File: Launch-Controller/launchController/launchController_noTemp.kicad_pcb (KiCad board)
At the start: 4 copper layers, 226 x 138.5 mm, 103 parts, among them J1 Conn_01x05_Pin, J10 Conn_01x05_Pin, J11 Raspberry_Pi_5, J13 26 pin Dsub, J14 DB25_Plug, J16 DB25_Plug, J17 DB25_Plug, J2 Conn_01x05_Pin, J3 Conn_01x05_Pin, J4 Conn_01x05_Pin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

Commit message: dimensions
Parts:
- C10, C11, C12, C13, C14, C2, C3, C4, C5, C6, C7, C8, C9: footprint Capacitor_THT:C_Disc_D5.1mm_W3.2mm_P5.00mm -> Capacitor_SMD:C_0402_1005Metric_Pad0.74x0.62mm_HandSolder
- D1, D13, D14, D15, D16, D17, D18, D19, D20, D21, D22: footprint LED_THT:LED_D4.0mm -> LED_SMD:LED_1206_3216Metric_Pad1.42x1.75mm_HandSolder
- D10, D11, D12, D2, D3, D4, D5, D6, D7, D8, D9: footprint LED_THT:LED_D3.0mm -> LED_SMD:LED_0603_1608Metric_Pad1.05x0.95mm_HandSolder
- Q1, Q10, Q2, Q3, Q4, Q5, Q6, Q7, Q8, Q9: footprint Package_TO_SOT_THT:TO-220-3_Horizontal_TabDown -> Package_TO_SOT_SMD:SOT-23-3
- R1, R10, R11, R12, R3, R4, R5, R6, R7, R8, R9: footprint Resistor_THT:R_Axial_DIN0411_L9.9mm_D3.6mm_P12.70mm_Horizontal -> Resistor_SMD:R_0805_2012Metric_Pad1.20x1.40mm_HandSolder
- R13, R14, R15, R16, R17, R18, R19, R2, R20, R21, R22, R23, R24, R25, R26, R27, R28, R29, R30, R31, R32: footprint Resistor_THT:R_Axial_DIN0207_L6.3mm_D2.5mm_P7.62mm_Horizontal -> Resistor_SMD:R_1210_3225Metric_Pad1.30x2.65mm_HandSolder
- U1, U2: footprint SARP:ADS1015 -> launch_controller:ADS1115
- moved C13 161.3 mm to (381.7, 309.0), turned to 0 degrees
- moved C12 132.2 mm to (381.7, 307.1), turned to 0 degrees
- moved C14 106.8 mm to (381.7, 311.0), turned to 0 degrees
- moved H4 28.7 mm to (196.9, 371.5)
- moved H2 28.3 mm to (403.4, 371.5)
- moved R23 26.3 mm to (371.2, 308.2), turned to 0 degrees
- moved D13 26.1 mm to (211.3, 364.0), turned to -90 degrees
- moved D3 25.7 mm to (218.7, 365.7)
- moved D14 25.3 mm to (230.6, 364.0), turned to -90 degrees
- moved D4 24.7 mm to (238.0, 365.7)
- moved D15 24.7 mm to (250.0, 364.0), turned to -90 degrees
- moved R24 24.3 mm to (371.2, 312.4), turned to 0 degrees
- moved D16 24.1 mm to (269.4, 364.0), turned to -90 degrees
- moved D5 23.8 mm to (257.4, 365.7)
- moved D17 23.6 mm to (288.8, 364.0), turned to -90 degrees
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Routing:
- net /+5V: track 765.3 -> 213.6 mm
- net /RelayOut1: track 245.0 -> 7.23 mm, vias 2 -> 0
- net /RelayOut2: track 222.9 -> 7.23 mm, vias 2 -> 0
- net /RelayOut3: track 203.8 -> 7.23 mm, vias 2 -> 0
- net /RelayOut4: track 189.7 -> 7.23 mm, vias 2 -> 0
- net /RelayOut5: track 158.4 -> 7.23 mm
- net /RelayOut6: track 136.9 -> 7.23 mm
- net /GPIO 4: track 117.8 -> 0.00 mm
- net /RelayOut7: track 112.1 -> 7.23 mm
- net /GPIO 17: track 101.9 -> 0.00 mm
- net /GPIO 13: track 95.1 -> 0.00 mm
- net /GPIO 27: track 83.5 -> 0.00 mm
- net /RelayOut8: track 90.0 -> 7.23 mm
- net /GPIO 6: track 76.1 -> 0.00 mm
- net /PressureSwitch_in3: track 71.9 -> 0.00 mm
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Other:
- board size 226 x 138.5 mm -> 228.5 x 138.5 mm
- board text added: "IN"
- board text added: "OUT"

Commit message: fixed edge cut
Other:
- board size 228.5 x 138.5 mm -> 219.9 x 107.1 mm
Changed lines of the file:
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@@
 		)
 		(property "Value" "LED"
-			(at 0 1.82 360)
+			(at 0 1.82 0)
 			(layer "F.Fab")
 			(effects
@@
 		)
 		(fp_text user "${REFERENCE}"
-			(at 0 0 360)
+			(at 0 0 0)
 			(layer "F.Fab")
 			(effects
@@
 		)
 		(property "Value" "1100Ω"
-			(at 0 2.28 360)
+			(at 0 2.28 0)
 			(layer "F.Fab")
 			(effects
@@
 		)
 		(fp_text user "${REFERENCE}"
-			(at 0 0 360)
+			(at 0 0 0)
 			(layer "F.Fab")
 			(effects
@@
 		)
 		(property "Value" "1100ohm"
-			(at 0 2.28 360)
+			(at 0 2.28 0)
 			(layer "F.Fab")
 			(effects
@@
 		)
 		(fp_text user "${REFERENCE}"
-			(at 0 0 360)
+			(at 0 0 0)
 			(layer "F.Fab")
 			(effects
@@
 		)
 		(property "Value" "LED"
-			(at 0 1.43 360)
+			(at 0 1.43 0)
 			(layer "F.Fab")
 			(effects
@@
 		)
 		(fp_text user "${REFERENCE}"
-			(at 0 0 360)
+			(at 0 0 0)
 			(layer "F.Fab")
 			(effects
@@
 		)
 		(fp_text user "${REFERENCE}"
-			(at 0 2.5 -90)
-			(unlocked yes)
+			(at 7.673391 -8.859263 0)
 			(layer "F.Fab")
 			(effects
@@
 		)
 		(fp_text user "${REFERENCE}"
-			(at 7.673391 -8.859263 0)
+			(at 0 2.5 -90)
+			(unlocked yes)
 			(layer "F.Fab")
 			(effects
@@
 		)
 		(fp_text user "${REFERENCE}"
-			(at 0 2.5 -90)
-			(unlocked yes)
+			(at 7.673391 -8.859263 0)
 			(layer "F.Fab")
 			(effects
@@
 		)
 		(fp_text user "${REFERENCE}"
-			(at 7.673391 -8.859263 0)
+			(at 0 2.5 -90)
+			(unlocked yes)
 			(layer "F.Fab")
 			(effects
@@
 		)
 		(fp_text user "${REFERENCE}"
-			(at 0 2.5 -90)
-			(unlocked yes)
+			(at 7.673391 -8.859263 0)
 			(layer "F.Fab")
 			(effects
@@
 		)
 		(fp_text user "${REFERENCE}"
-			(at 7.673391 -8.859263 0)
+			(at 0 2.5 -90)
+			(unlocked yes)
 			(layer "F.Fab")
 			(effects
@@
 		)
 		(property "Value" "0.1uF"
-			(at 0 1.16 360)
+			(at 0 1.16 0)
 			(layer "F.Fab")
 			(effects
@@
 		)
 		(fp_text user "${REFERENCE}"
-			(at 0 0 360)
+			(at 0 0 0)
 			(layer "F.Fab")
 			(effects
@@
 		)
 		(fp_text user "${REFERENCE}"
-			(at 0 2.5 -90)
-			(unlocked yes)
+			(at 7.673391 -8.859263 0)
 			(layer "F.Fab")
 			(effects
@@
 		)
 		(fp_text user "${REFERENCE}"
-			(at 7.673391 -8.859263 0)
+			(at 0 2.5 -90)
+			(unlocked yes)
 			(layer "F.Fab")
 			(effects
@@
 		)
 		(property "Value" "LED"
-			(at 0 1.43 360)
+			(at 0 1.43 0)
 			(layer "F.Fab")
 			(effects
@@
 		)
 		(fp_text user "${REFERENCE}"
-			(at 0 0 360)
+			(at 0 0 0)
 			(layer "F.Fab")
 			(effects
@@
 		(tags "CONN")
 		(property "Reference" "J11"
-			(at 44.45 -34.29 360)
+			(at 44.45 -34.29 0)
 			(layer "F.Fab")
 			(effects
@@
 		)
 		(property "Value" "Raspberry_Pi_5"
-			(at 44.45 -29.21 360)
+			(at 44.45 -29.21 0)
 			(layer "F.Fab")
 			(effects
@@
 		)
 		(property "Footprint" "Raspberry-Pi-4-library-for-kicad:RPi_5_upside_down"
-			(at 52.07 -52.07 360)
+			(at 52.07 -52.07 0)
 			(layer "F.Fab")
 			(hide yes)
@@
 		)
 		(property "Datasheet" "https://datasheets.raspberrypi.com/rp1/rp1-peripherals.pdf"
-			(at 52.07 -52.07 360)
+			(at 52.07 -52.07 0)
 			(layer "F.Fab")
 			(hide yes)
@@
 		)
 		(property "Description" "Raspberry Pi 5 Model B - 4GB"
-			(at 52.07 -52.07 360)
+			(at 52.07 -52.07 0)
 			(layer "F.Fab")
 			(hide yes)
@@
 		)
 	)
-	(gr_line
-		(start 181.5 409.9)
-		(end 193.4 410)
-		(stroke
-			(width 0.05)
-			(type default)
-		)
-		(layer "Edge.Cuts")
-	)
 	(gr_rect

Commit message: lc final draft
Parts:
- added D23: 5KPxxCA, Diode_SMD:D_SOD-923, F.Cu at (213.3, 367.4)
- added D24: 5KPxxCA, Diode_SMD:D_SOD-923, F.Cu at (232.8, 367.4)
- added D25: 5KPxxCA, Diode_SMD:D_SOD-923, F.Cu at (252.2, 367.4)
- added D26: 5KPxxCA, Diode_SMD:D_SOD-923, F.Cu at (271.6, 367.4)
- added D27: 5KPxxCA, Diode_SMD:D_SOD-923, F.Cu at (291.0, 367.4)
- added D28: 5KPxxCA, Diode_SMD:D_SOD-923, F.Cu at (310.4, 367.4)
- added D29: 5KPxxCA, Diode_SMD:D_SOD-923, F.Cu at (329.8, 367.4)
- added D30: 5KPxxCA, Diode_SMD:D_SOD-923, F.Cu at (349.0, 367.4)
- added D31: 5KPxxCA, Diode_SMD:D_SOD-923, F.Cu at (368.4, 367.4)
- added D32: 5KPxxCA, Diode_SMD:D_SOD-923, F.Cu at (387.9, 367.4)
- added D33: 5KPxxCA, Diode_SMD:D_SOD-523, F.Cu at (253.7, 285.7)
- added D34: 5KPxxCA, Diode_SMD:D_SOD-523, F.Cu at (249.4, 285.7)
- added D35: 5KPxxCA, Diode_SMD:D_SOD-523, F.Cu at (245.1, 285.7)
- added D36: 5KPxxCA, Diode_SMD:D_SOD-523, F.Cu at (240.7, 285.7)
- added D37: 5KPxxCA, Diode_SMD:D_SOD-523, F.Cu at (236.4, 285.7)
- added D38: 5KPxxCA, Diode_SMD:D_SOD-523, F.Cu at (232.0, 285.7)
- added D39: 5KPxxCA, Diode_SMD:D_SOD-523, F.Cu at (227.7, 285.7)
- added D40: 5KPxxCA, Diode_SMD:D_SOD-523, F.Cu at (223.3, 285.7)
- added D41: 5KPxxA, Diode_SMD:D_SOD-323_HandSoldering, F.Cu at (273.3, 286.0)
- added G***: LOGO, kicad_import:avionicslogo, F.Cu at (220.3, 322.3)
- added G***: LOGO, kicad_import:small shield, F.Cu at (403.3, 353.5)
- added G1: LOGO, kicad_import:round sarp, F.Cu at (242.5, 328.6)
- added J15: Conn_01x03_Pin, Package_TO_SOT_SMD:SOT-23-3, F.Cu at (210.7, 297.6)
- added J18: Conn_01x03_Pin, Package_TO_SOT_SMD:SOT-23-3, F.Cu at (209.6, 353.5)
- moved C12 158.5 mm to (223.2, 308.7)
- moved C13 131.7 mm to (250.0, 308.7)
- moved C14 109.0 mm to (278.1, 344.6), turned to 90 degrees
- moved R32 80.4 mm to (305.9, 287.8), turned to 90 degrees
- moved R31 73.9 mm to (311.1, 287.8), turned to 90 degrees
- moved R30 67.4 mm to (316.2, 287.8), turned to 90 degrees
- moved R29 61.0 mm to (321.4, 287.8), turned to 90 degrees
- moved R28 54.6 mm to (326.6, 287.8), turned to 90 degrees
- moved R27 54.3 mm to (331.7, 287.8), turned to 90 degrees
- moved R26 47.6 mm to (336.9, 287.8), turned to 90 degrees
- moved R25 41.0 mm to (342.1, 287.8), turned to 90 degrees
- moved R24 34.4 mm to (347.2, 287.8), turned to 90 degrees
- moved R23 27.8 mm to (352.4, 287.8), turned to 90 degrees
- moved D1 4.28 mm to (284.4, 287.4)
- moved C15 4.21 mm to (209.6, 349.1)
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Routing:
- net /+5V: track 213.6 -> 1001.6 mm, vias 0 -> 11
- net GND: track 0.00 -> 448.6 mm, vias 0 -> 1
- net /RelayOut1: track 7.23 -> 227.1 mm, vias 0 -> 2
- net /RelayOut2: track 7.23 -> 206.3 mm, vias 0 -> 2
- net /RelayOut3: track 7.23 -> 185.8 mm, vias 0 -> 2
- net /RelayOut4: track 7.23 -> 165.1 mm, vias 0 -> 2
- net /guarded_RelayOut10: track 0.00 -> 146.0 mm, vias 0 -> 1
- net /RelayOut5: track 7.23 -> 144.6 mm, vias 0 -> 2
- net /guarded_RelayOut9: track 0.00 -> 135.9 mm, vias 0 -> 1
- net /guarded_RelayOut8: track 0.67 -> 126.8 mm, vias 0 -> 1
- net /guarded_RelayOut7: track 0.00 -> 118.3 mm, vias 0 -> 1
- net /RelayOut6: track 7.23 -> 124.0 mm, vias 0 -> 2
- net /guarded_RelayOut6: track 0.42 -> 111.4 mm, vias 0 -> 1
- net /guarded_RelayOut5: track 0.00 -> 101.5 mm, vias 0 -> 1
- net /SCL: track 0.00 -> 96.3 mm
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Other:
- board text added: "2025"
- board text added: "Cooper Reynolds"
- board text added: "Launch Controller v2.0"
- board text added: "Society for Advanced Rocket Propulsion"

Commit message: pretty board
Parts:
- moved H1 0.57 mm to (403.1, 278.4), turned to 90 degrees
- moved H3 0.47 mm to (197.1, 278.4)
- moved H2 0.38 mm to (403.1, 371.6)
- moved H4 0.21 mm to (197.1, 371.6)
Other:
- board text added: "BUCK CONVERTER"
- board text added: "Buck Converter Connector"
- board text added: "LED Indication Connector"
- board text added: "Power Arm Connector"
- board text added: "Power Connector"
- board text added: "Pressure Transducer Connector"
- board text added: "RELAY 1"
- board text added: "RELAY 10"
- board text added: "RELAY 2"
- board text added: "RELAY 3"
- board text added: "RELAY 4"
- board text added: "RELAY 5"
- board text added: "RELAY 6"
- board text added: "RELAY 7"
- board text added: "RELAY 8"
- board text added: "RELAY 9"
- board text added: "Relay Connector"
- board text added: "Relay Connectors 1-10"
- board text added: "Safeguard Connector"

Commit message: LC cosmetic updates
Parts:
- moved J12 219.2 mm to (233.4, 47.5), turned to 180 degrees
- moved D41 216.2 mm to (180.0, 91.0), turned to 0 degrees
- moved D2 212.2 mm to (185.9, 95.5)
- moved D1 211.7 mm to (195.1, 95.4)
- moved C1 211.6 mm to (116.3, 102.0)
- moved D10 211.6 mm to (259.6, 174.9)
- moved D11 211.6 mm to (279.0, 174.9)
- moved D12 211.6 mm to (298.4, 174.9)
- moved D3 211.6 mm to (123.9, 174.9)
- moved D4 211.6 mm to (143.3, 174.9)
- moved D5 211.6 mm to (162.7, 174.9)
- moved D6 211.6 mm to (182.1, 174.9)
- moved D7 211.6 mm to (201.6, 174.9)
- moved D8 211.6 mm to (221.0, 174.9)
- moved D9 211.6 mm to (240.4, 174.9)
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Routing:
- net GND: track 448.6 -> 466.6 mm
- net /+5V: track 1001.6 -> 1007.6 mm
- net Net-(D2-A): track 5.90 -> 2.63 mm
- net /+24V: track 16.0 -> 17.0 mm

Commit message: polished launch controller layout
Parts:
- J1, J10, J2, J3, J4, J5, J6, J7, J8, J9: footprint launch_controller:Relay Connector -> launch_controller:RelaySwitch Connector
- moved J7 4.52 mm to (222.1, 176.1)
- moved J6 4.51 mm to (202.7, 176.1)
- moved J5 4.50 mm to (183.3, 176.1)
- moved J4 4.49 mm to (163.9, 176.1)
- moved J3 4.48 mm to (144.5, 176.1)
- moved J2 4.47 mm to (125.1, 176.1)
- moved J1 4.46 mm to (105.7, 176.1)
- moved J10 4.36 mm to (280.3, 176.1)
- moved J9 4.35 mm to (260.9, 176.1)
- moved J8 4.34 mm to (241.5, 176.1)
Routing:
- net GND: track 466.6 -> 465.7 mm

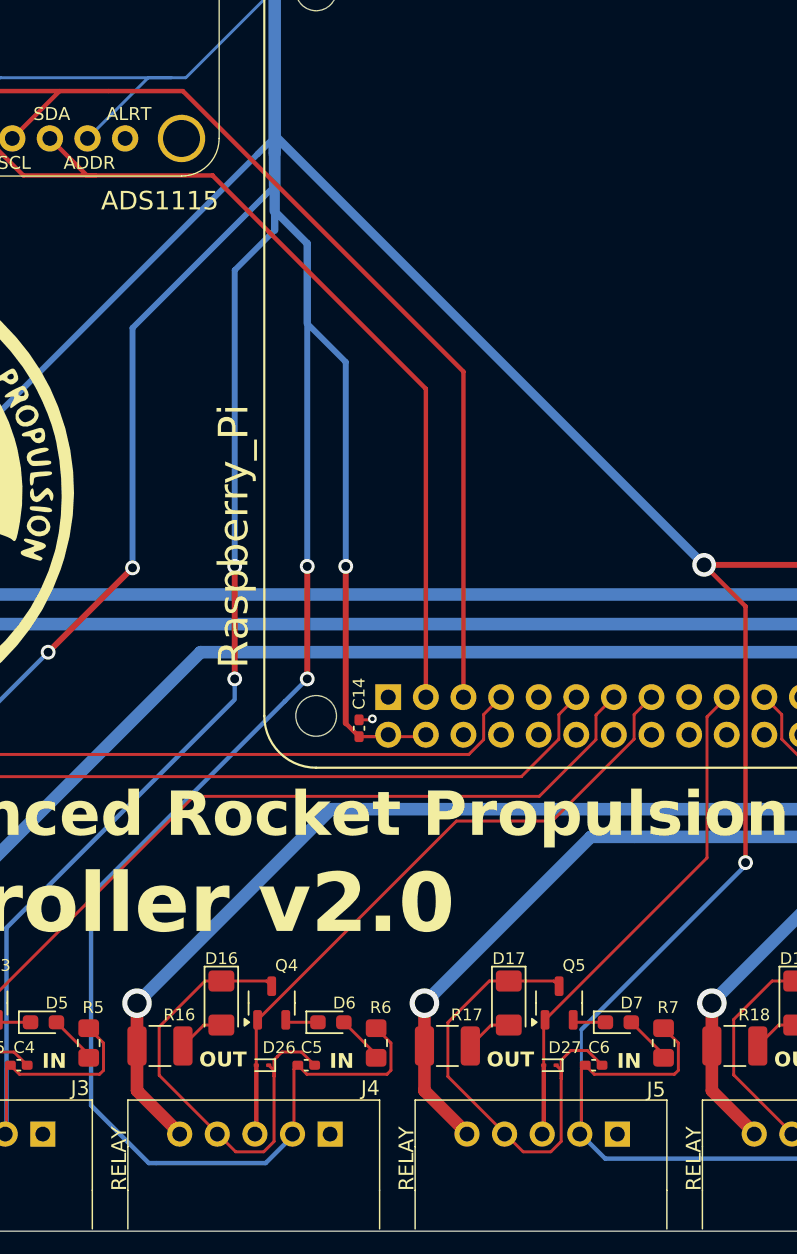
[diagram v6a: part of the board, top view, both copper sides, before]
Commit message: logic shifter in LC, cleaning up buck_5v
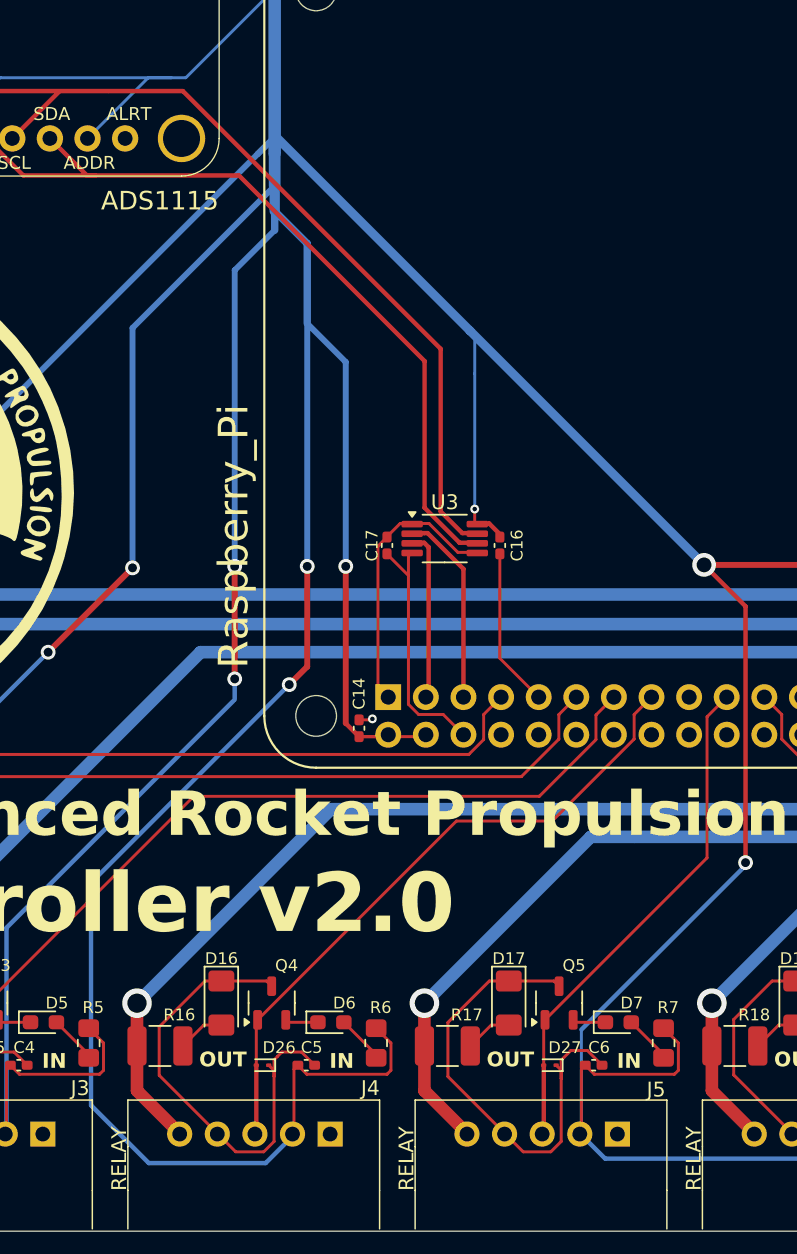
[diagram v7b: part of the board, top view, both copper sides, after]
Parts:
- added C16: 0.1uF, Capacitor_SMD:C_0402_1005Metric_Pad0.74x0.62mm_HandSolder, F.Cu at (193.5, 142.7)
- added C17: 0.1uF, Capacitor_SMD:C_0402_1005Metric_Pad0.74x0.62mm_HandSolder, F.Cu at (185.9, 142.7)
- added U3: TCA9517ADGK, Package_SO:Texas_S-PDSO-G8_3x3mm_P0.65mm, F.Cu at (189.8, 142.3)
- D23, D24, D25, D26, D27, D28, D29, D30, D31, D32, D33, D34, D35, D36, D37, D38, D39, D40: value 5KPxxCA -> TVS Diode
- D41: value 5KPxxA -> TVS Diode
- J1, J10, J2, J3, J4, J5, J6, J7, J8, J9: value Conn_01x05_Pin -> Relay Connector
- J12: value ~ -> Buck Connector
- J15, J18: value Conn_01x03_Pin -> TVS Diode
- POWER1, RELAY_ARM1: value Conn_01x03_Pin -> Power Connector
- R1: value 150ohm -> 150Ω
- R13, R14, R15, R16, R17, R18, R19, R20, R21, R22: value 1100Ω -> 1100Ω
- R2, R23, R24, R25, R26, R27, R28, R29, R30, R31, R32: value 1100ohm -> 1100Ω
- U1, U2: value ADS1015IDGS -> ADS1115
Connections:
- J11 pad 1: unconnected-(J11-3V3-Pad1)_1 -> /+3.3V
- J11 pad 17: unconnected-(J11-3V3-Pad1) -> /+3.3V
- J11 pad 3: /SDA -> /SDAA
- J11 pad 5: /SCL -> /SCLA
- U1 pad 3: /SCL -> /SCLB
- U1 pad 4: /SDA -> /SDAB
- U2 pad 3: /SCL -> /SCLB
- U2 pad 4: /SDA -> /SDAB
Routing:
- net /SCL: track 96.3 -> 0.00 mm
- net /SDA: track 86.7 -> 0.00 mm
- net /SCLB: track 0.00 -> 86.0 mm
- net /SDAB: track 0.00 -> 79.3 mm
- net GND: track 465.7 -> 493.5 mm
- net /+3.3V: track 0.00 -> 18.3 mm
- net /+5V: track 1007.6 -> 1022.9 mm, vias 11 -> 12
- net /SCLA: track 0.00 -> 13.1 mm
- net /SDAA: track 0.00 -> 11.4 mm
